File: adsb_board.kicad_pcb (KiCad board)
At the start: 2 copper layers, 50 x 50 mm, 7 parts, among them J1 Conn_Coaxial, J2 Conn_Coaxial, U1 TA1090EC

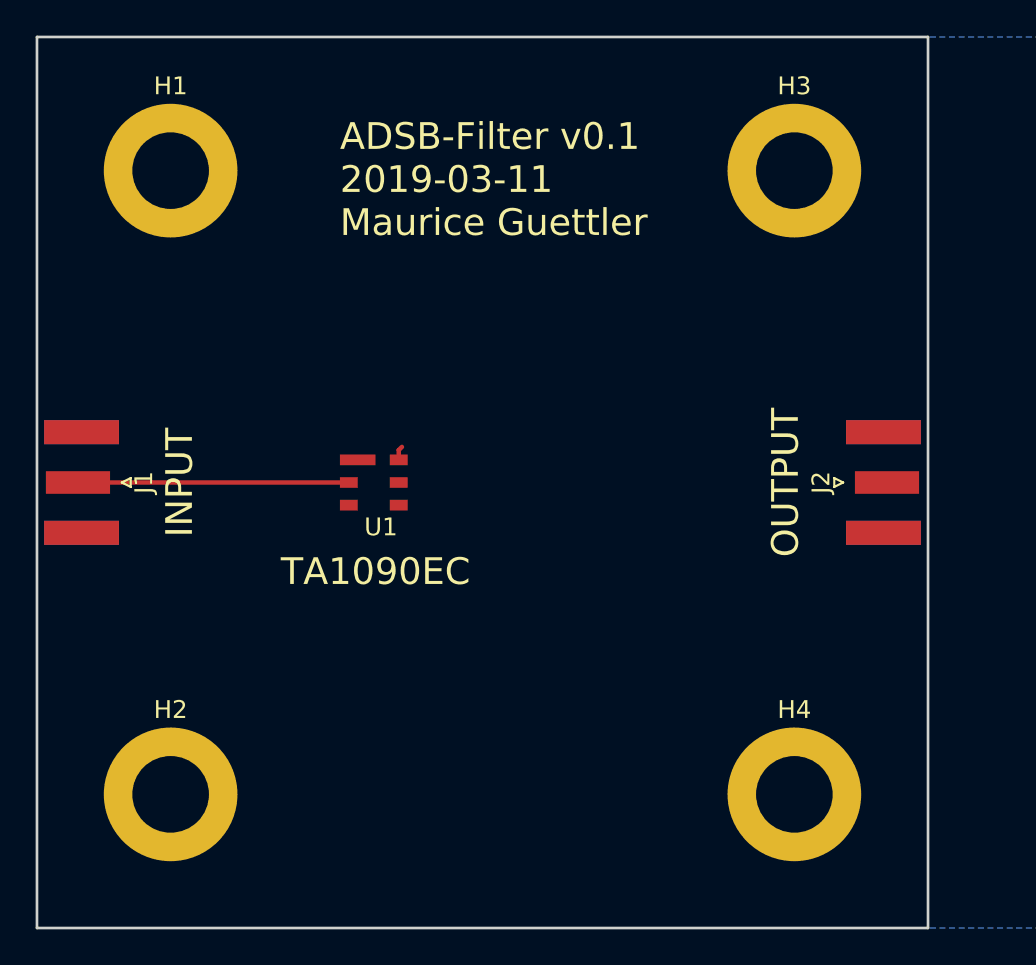
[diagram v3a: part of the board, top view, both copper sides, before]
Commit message: reduced size further to 50x25mm
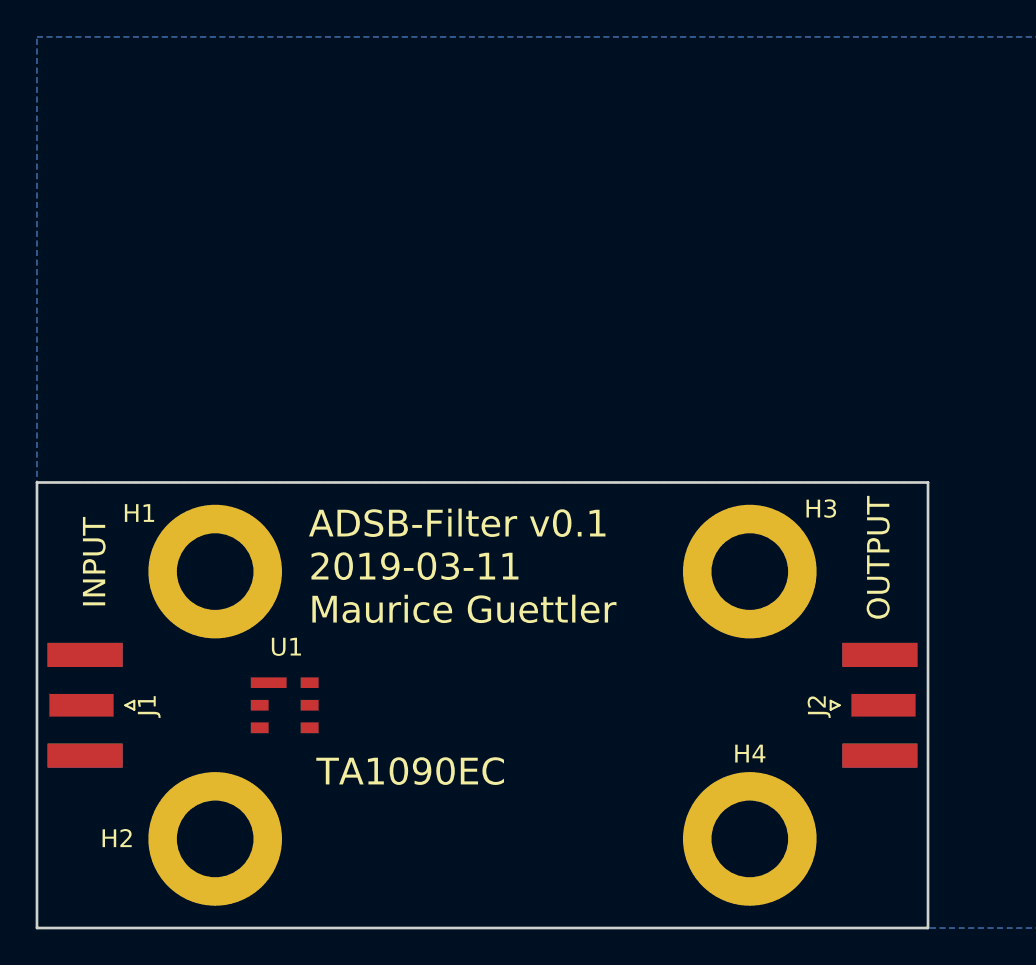
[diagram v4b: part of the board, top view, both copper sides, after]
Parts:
- moved H1 22.6 mm to (110.0, 80.0)
- moved H3 22.6 mm to (140.0, 80.0)
- moved U1 13.5 mm to (113.9, 87.5)
- moved J1 12.5 mm to (102.7, 87.5)
- moved J2 12.5 mm to (147.3, 87.5)
- moved H2 3.54 mm to (110.0, 95.0)
- moved H4 3.54 mm to (140.0, 95.0)
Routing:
- net Net-(J1-Pad1): track 15.2 -> 0.00 mm
- net GND: track 0.80 -> 0.00 mm
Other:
- board size 50 x 50 mm -> 50 x 25 mm
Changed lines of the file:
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@@
     (thickness 1.6)
     (drawings 8)
-    (tracks 3)
+    (tracks 0)
     (zones 0)
     (modules 7)
@@
   )
   (module Connector_Coaxial:SMA_Samtec_SMA-J-P-H-ST-EM1_EdgeMount (layer F.Cu)
-    (at 147.5 75)
+    (at 147.3 87.5)
     (descr http://suddendocs.samtec.com/prints/sma-j-p-x-st-em1-mkt.pdf)
     (tags SMA)
@@
   )
   (module Connector_Coaxial:SMA_Samtec_SMA-J-P-H-ST-EM1_EdgeMount (layer F.Cu)
-    (at 102.5 75 180)
+    (at 102.7 87.5 180)
     (descr http://suddendocs.samtec.com/prints/sma-j-p-x-st-em1-mkt.pdf)
     (tags SMA)
@@
   )
   (module Filter:ta1090ec (layer F.Cu)
-    (at 118.9 75)
-    (fp_text reference U1 (at 0.4 2.5) (layer F.SilkS)
+    (at 113.9 87.5)
+    (fp_text reference U1 (at 0.1 -3.25) (layer F.SilkS)
       (effects (font (size 1 1) (thickness 0.15)))
     )
@@
   )
   (module MountingHole:MountingHole_4.3mm_M4_DIN965_Pad (layer F.Cu)
-    (at 142.5 92.5)
+    (at 140 95)
     (descr "Mounting Hole 4.3mm, M4, DIN965")
     (tags "mounting hole 4.3mm m4 din965")
@@
   )
   (module MountingHole:MountingHole_4.3mm_M4_DIN965_Pad (layer F.Cu)
-    (at 142.5 57.5)
+    (at 140 80)
     (descr "Mounting Hole 4.3mm, M4, DIN965")
     (tags "mounting hole 4.3mm m4 din965")
     (attr virtual)
-    (fp_text reference H3 (at 0 -4.75) (layer F.SilkS)
+    (fp_text reference H3 (at 4 -3.5) (layer F.SilkS)
       (effects (font (size 1 1) (thickness 0.15)))
     )
@@
   )
   (module MountingHole:MountingHole_4.3mm_M4_DIN965_Pad (layer F.Cu)
-    (at 107.5 92.5)
+    (at 110 95)
     (descr "Mounting Hole 4.3mm, M4, DIN965")
     (tags "mounting hole 4.3mm m4 din965")
     (attr virtual)
-    (fp_text reference H2 (at 0 -4.75) (layer F.SilkS)
+    (fp_text reference H2 (at -5.5 0) (layer F.SilkS)
       (effects (font (size 1 1) (thickness 0.15)))
     )
@@
   )
   (module MountingHole:MountingHole_4.3mm_M4_DIN965_Pad (layer F.Cu)
-    (at 107.5 57.5)
+    (at 110 80)
     (descr "Mounting Hole 4.3mm, M4, DIN965")
     (tags "mounting hole 4.3mm m4 din965")
     (attr virtual)
-    (fp_text reference H1 (at 0 -4.75) (layer F.SilkS)
+    (fp_text reference H1 (at -4.25 -3.25) (layer F.SilkS)
       (effects (font (size 1 1) (thickness 0.15)))
     )
@@
       (net 3 GND))
   )
-  (gr_text TA1090EC (at 119 80) (layer F.SilkS)
+  (gr_text TA1090EC (at 121 91.25) (layer F.SilkS)
     (effects (font (size 1.5 1.5) (thickness 0.3)))
   )
-  (gr_text OUTPUT (at 142 75 90) (layer F.SilkS)
-    (effects (font (size 1.5 1.5) (thickness 0.3)))
-  )
-  (gr_text INPUT (at 108 75 90) (layer F.SilkS)
-    (effects (font (size 1.5 1.5) (thickness 0.3)))
-  )
-  (gr_text "ADSB-Filter v0.1\n2019-03-11\nMaurice Guettler" (at 117 58) (layer F.SilkS)
+  (gr_text OUTPUT (at 147.25 79.25 90) (layer F.SilkS)
+    (effects (font (size 1.25 1.25) (thickness 0.3)))
+  )
+  (gr_text INPUT (at 103.25 79.5 90) (layer F.SilkS)
+    (effects (font (size 1.25 1.25) (thickness 0.3)))
+  )
+  (gr_text "ADSB-Filter v0.1\n2019-03-11\nMaurice Guettler" (at 115.25 79.75) (layer F.SilkS)
     (effects (font (size 1.5 1.5) (thickness 0.3)) (justify left))
   )
-  (gr_line (start 100 50) (end 100 100) (layer Edge.Cuts) (width 0.15))
-  (gr_line (start 150 50) (end 100 50) (layer Edge.Cuts) (width 0.15))
-  (gr_line (start 150 100) (end 150 50) (layer Edge.Cuts) (width 0.15))
+  (gr_line (start 100 75) (end 100 100) (layer Edge.Cuts) (width 0.15))
+  (gr_line (start 150 75) (end 100 75) (layer Edge.Cuts) (width 0.15))
+  (gr_line (start 150 100) (end 150 75) (layer Edge.Cuts) (width 0.15))
   (gr_line (start 100 100) (end 150 100) (layer Edge.Cuts) (width 0.15))
-  (segment (start 102.3 75) (end 117.5 75) (width 0.25) (layer F.Cu) (net 2))
-  (segment (start 120.3 73.18) (end 120.48 73) (width 0.25) (layer F.Cu) (net 3))
-  (segment (start 120.3 73.73) (end 120.3 73.18) (width 0.25) (layer F.Cu) (net 3))
   (zone (net 3) (net_name GND) (layer F.Cu) (hatch edge 0.508)
     (connect_pads (clearance 0.508))
@@
     (polygon
       (pts
-        (xy 100 50) (xy 150 50) (xy 150 100) (xy 100 100)
+        (xy 100 75) (xy 150 75) (xy 150 100) (xy 100 100)
       )
     )

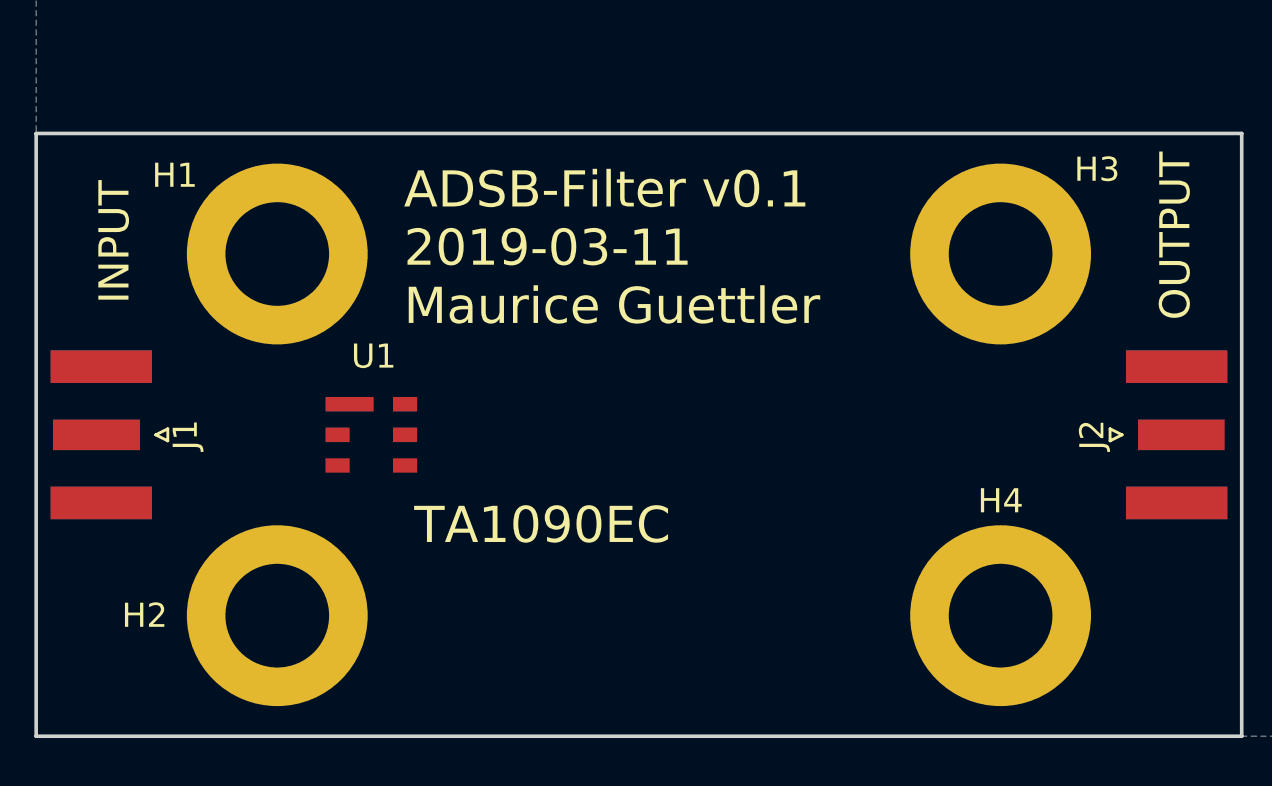
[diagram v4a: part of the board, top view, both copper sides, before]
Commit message: remove two mounting holes
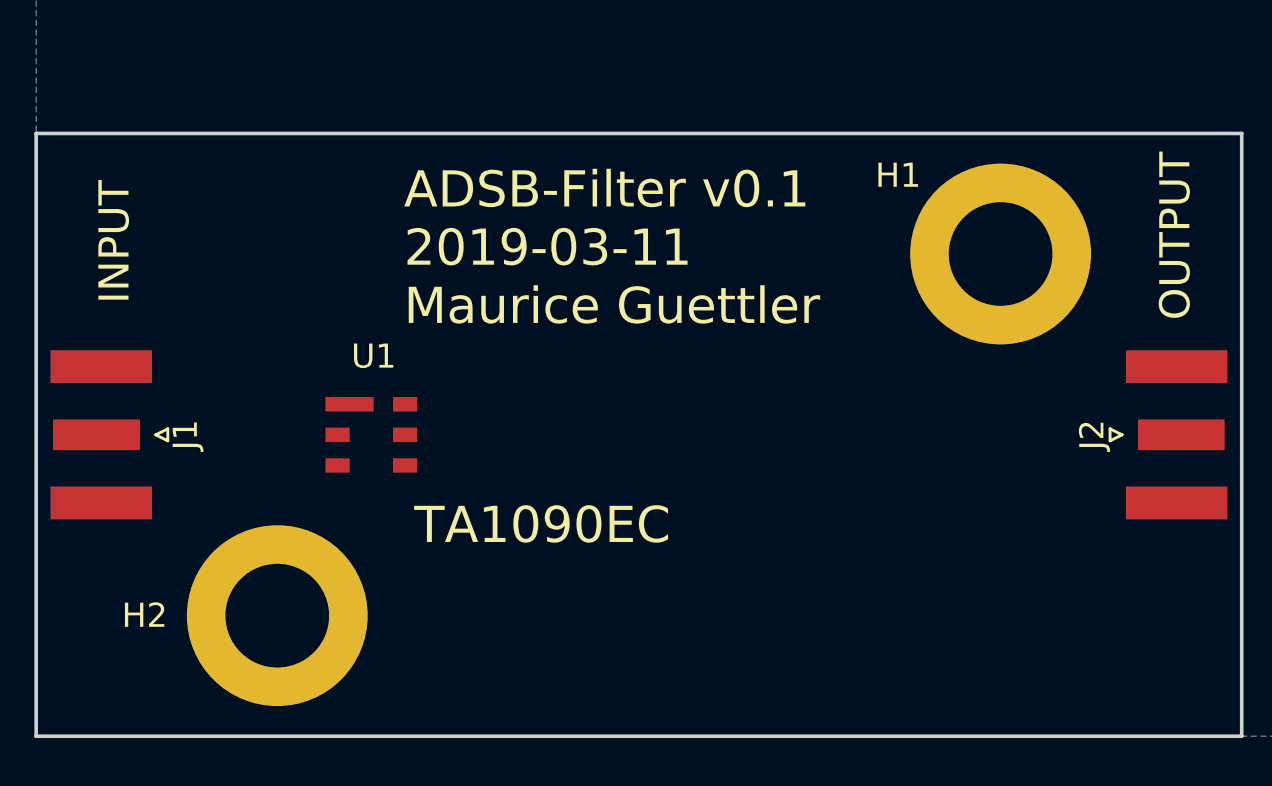
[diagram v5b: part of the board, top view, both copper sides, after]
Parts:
- removed H3, H4: MountingHole_Pad, MountingHole:MountingHole_4.3mm_M4_DIN965_Pad
- moved H1 30.0 mm to (140.0, 80.0)
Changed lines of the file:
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@@
     (tracks 0)
     (zones 0)
-    (modules 7)
+    (modules 5)
     (nets 4)
   )
@@
   )
   (module MountingHole:MountingHole_4.3mm_M4_DIN965_Pad (layer F.Cu)
-    (at 140 95)
-    (descr "Mounting Hole 4.3mm, M4, DIN965")
-    (tags "mounting hole 4.3mm m4 din965")
-    (attr virtual)
-    (fp_text reference H4 (at 0 -4.75) (layer F.SilkS)
-      (effects (font (size 1 1) (thickness 0.15)))
-    )
-    (fp_text value MountingHole_Pad (at 0 4.75) (layer F.Fab)
-      (effects (font (size 1 1) (thickness 0.15)))
-    )
-    (fp_circle (center 0 0) (end 4 0) (layer F.CrtYd) (width 0.05))
-    (fp_circle (center 0 0) (end 3.75 0) (layer Cmts.User) (width 0.15))
-    (fp_text user %R (at 0.3 0) (layer F.Fab)
-      (effects (font (size 1 1) (thickness 0.15)))
-    )
-    (pad 1 thru_hole circle (at 0 0) (size 7.5 7.5) (drill 4.3) (layers *.Cu *.Mask)
-      (net 3 GND))
-  )
-  (module MountingHole:MountingHole_4.3mm_M4_DIN965_Pad (layer F.Cu)
-    (at 140 80)
-    (descr "Mounting Hole 4.3mm, M4, DIN965")
-    (tags "mounting hole 4.3mm m4 din965")
-    (attr virtual)
-    (fp_text reference H3 (at 4 -3.5) (layer F.SilkS)
-      (effects (font (size 1 1) (thickness 0.15)))
-    )
-    (fp_text value MountingHole_Pad (at 0 4.75) (layer F.Fab)
-      (effects (font (size 1 1) (thickness 0.15)))
-    )
-    (fp_text user %R (at 0.3 0) (layer F.Fab)
-      (effects (font (size 1 1) (thickness 0.15)))
-    )
-    (fp_circle (center 0 0) (end 3.75 0) (layer Cmts.User) (width 0.15))
-    (fp_circle (center 0 0) (end 4 0) (layer F.CrtYd) (width 0.05))
-    (pad 1 thru_hole circle (at 0 0) (size 7.5 7.5) (drill 4.3) (layers *.Cu *.Mask)
-      (net 3 GND))
-  )
-  (module MountingHole:MountingHole_4.3mm_M4_DIN965_Pad (layer F.Cu)
     (at 110 95)
     (descr "Mounting Hole 4.3mm, M4, DIN965")
@@
   )
   (module MountingHole:MountingHole_4.3mm_M4_DIN965_Pad (layer F.Cu)
-    (at 110 80)
+    (at 140 80)
     (descr "Mounting Hole 4.3mm, M4, DIN965")
     (tags "mounting hole 4.3mm m4 din965")

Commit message: routed first draft of adsb-board
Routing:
- net Net-(J2-Pad1): track 0.00 -> 32.2 mm
- net Net-(J1-Pad1): track 0.00 -> 10.0 mm
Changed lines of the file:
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@@
     (thickness 1.6)
     (drawings 8)
-    (tracks 0)
+    (tracks 2)
     (zones 0)
     (modules 5)
@@
   (gr_line (start 150 100) (end 150 75) (layer Edge.Cuts) (width 0.15))
   (gr_line (start 100 100) (end 150 100) (layer Edge.Cuts) (width 0.15))
+  (segment (start 115.3 87.5) (end 147.5 87.5) (width 0.25) (layer F.Cu) (net 1))
+  (segment (start 102.5 87.5) (end 112.5 87.5) (width 0.25) (layer F.Cu) (net 2))
   (zone (net 3) (net_name GND) (layer F.Cu) (hatch edge 0.508)
     (connect_pads (clearance 0.508))

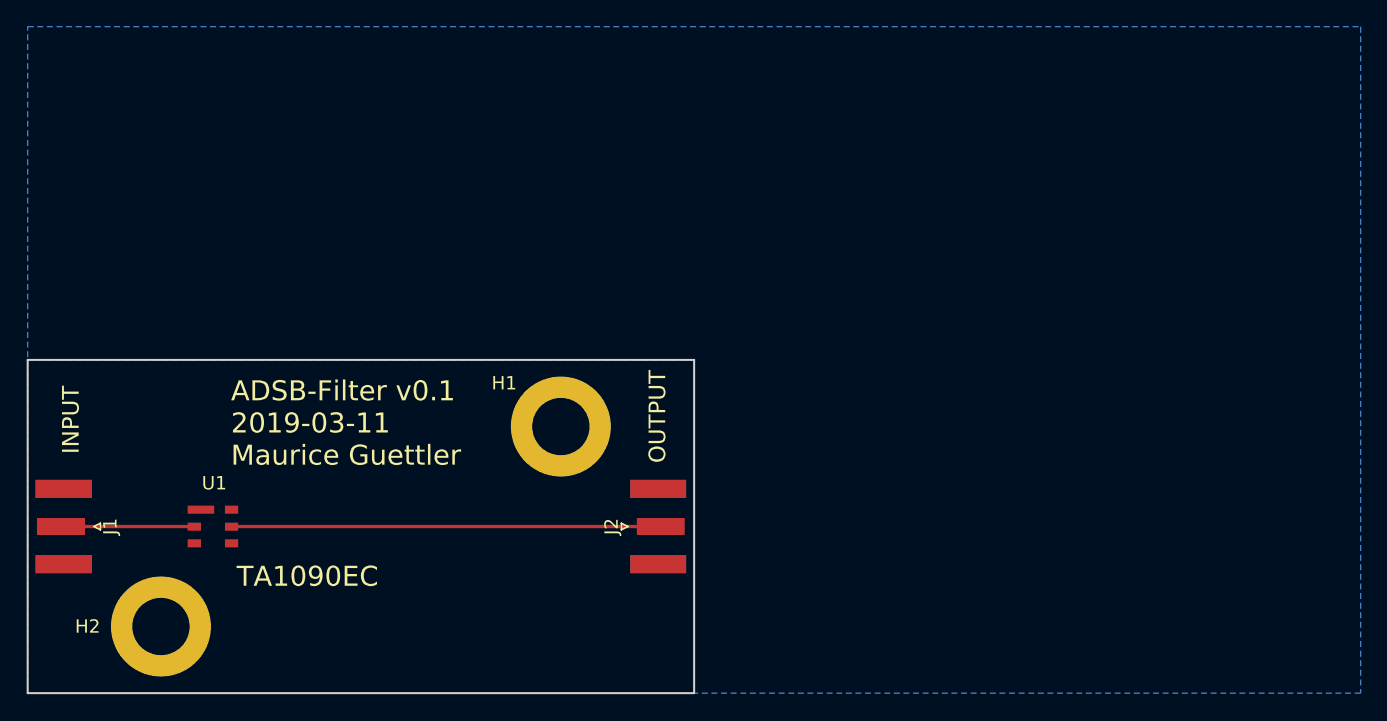
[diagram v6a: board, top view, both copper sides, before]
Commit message: place new components
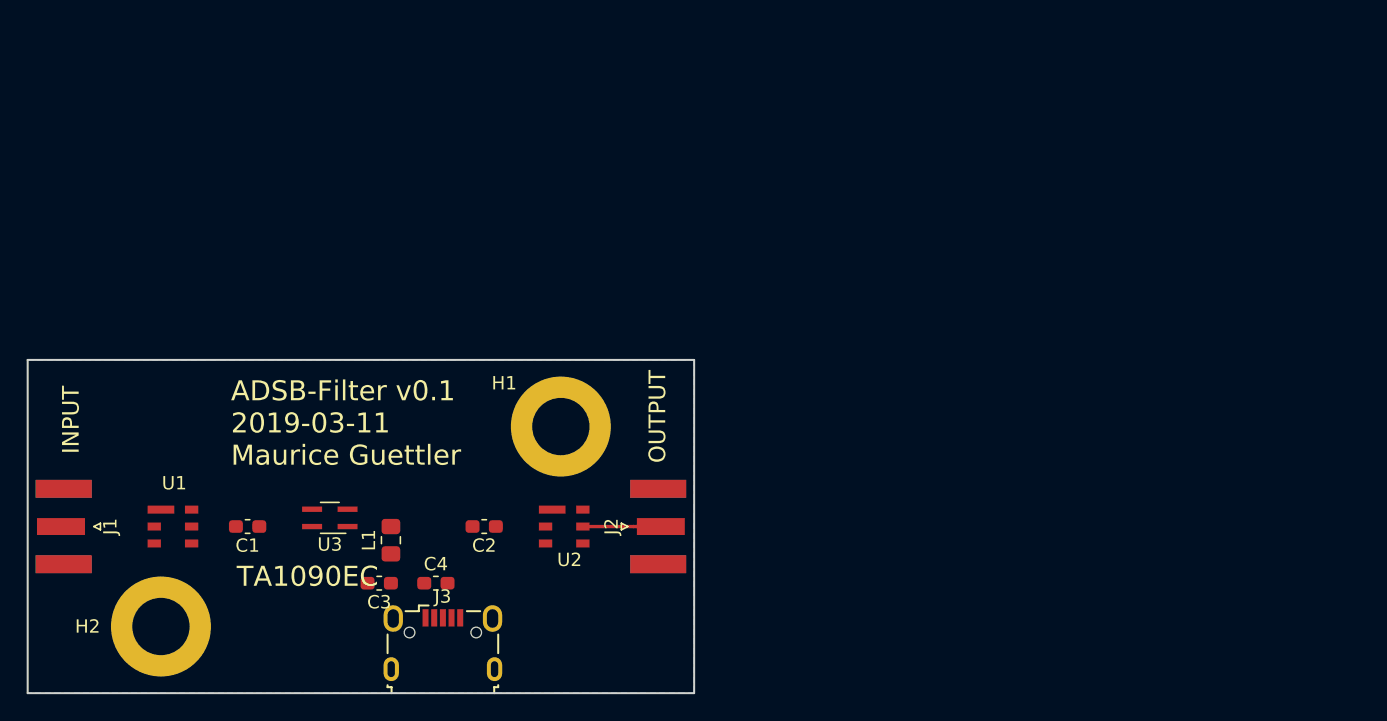
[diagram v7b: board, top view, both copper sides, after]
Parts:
- added C1: 150pF, Capacitor_SMD:C_0603_1608Metric_Pad1.05x0.95mm_HandSolder, F.Cu at (116.5, 87.5)
- added C2: 150pF, Capacitor_SMD:C_0603_1608Metric_Pad1.05x0.95mm_HandSolder, F.Cu at (134.2, 87.5)
- added C3: 1000pF, Capacitor_SMD:C_0603_1608Metric_Pad1.05x0.95mm_HandSolder, F.Cu at (126.4, 91.8)
- added C4: 4.7uF, Capacitor_SMD:C_0603_1608Metric_Pad1.05x0.95mm_HandSolder, F.Cu at (130.6, 91.8)
- added J3: USB_B_Micro, Connector_USB:USB_Micro-B_Wuerth_629105150521, F.Cu at (131.2, 96.2)
- added L1: 22nH, Inductor_SMD:L_0805_2012Metric_Pad1.15x1.40mm_HandSolder, F.Cu at (127.2, 88.5)
- added U2: TA1090EC, Filter:ta1090ec, F.Cu at (140.2, 87.5)
- added U3: PSA4-5043+, Package_TO_SOT_SMD:SOT-343_SC-70-4_Handsoldering, F.Cu at (122.7, 86.8)
- moved U1 3.00 mm to (110.9, 87.5)
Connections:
- net GND renamed /GND
- net Net-(J1-Pad1) renamed /INPUT
- J2 pad 1: Net-(J2-Pad1) -> /OUTPUT
- U1 pad 5: Net-(J2-Pad1) -> Net-(C1-Pad2)
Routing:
- net Net-(J2-Pad1): track 32.2 -> 0.00 mm
- net /INPUT: track 10.0 -> 0.00 mm
- net /OUTPUT: track 0.00 -> 5.85 mm
- removed copper zone on F.Cu, net /GND
